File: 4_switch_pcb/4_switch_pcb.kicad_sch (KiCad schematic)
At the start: 11 parts, among them J1 USB_B_Micro, SW1 SW_Push, U1 ATmega32U4-A, Y1 Crystal_GND2_Small

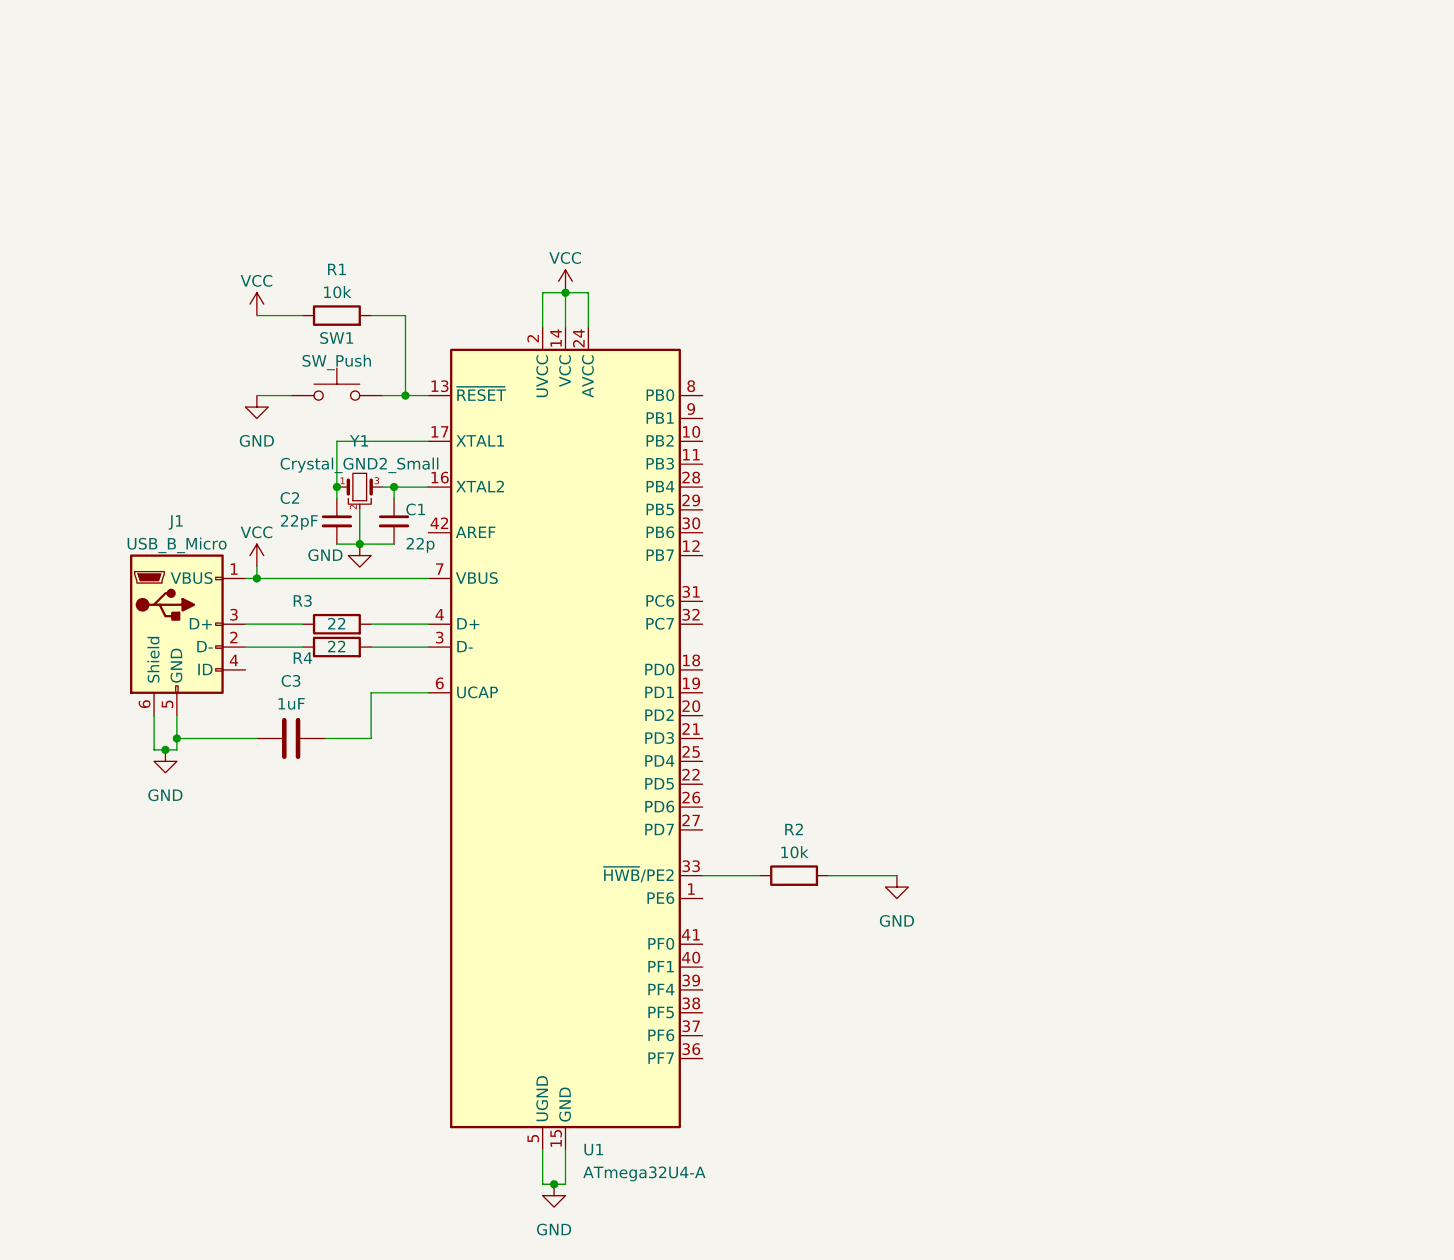
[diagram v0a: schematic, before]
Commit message: feat: add switch matrix, isp and header pins
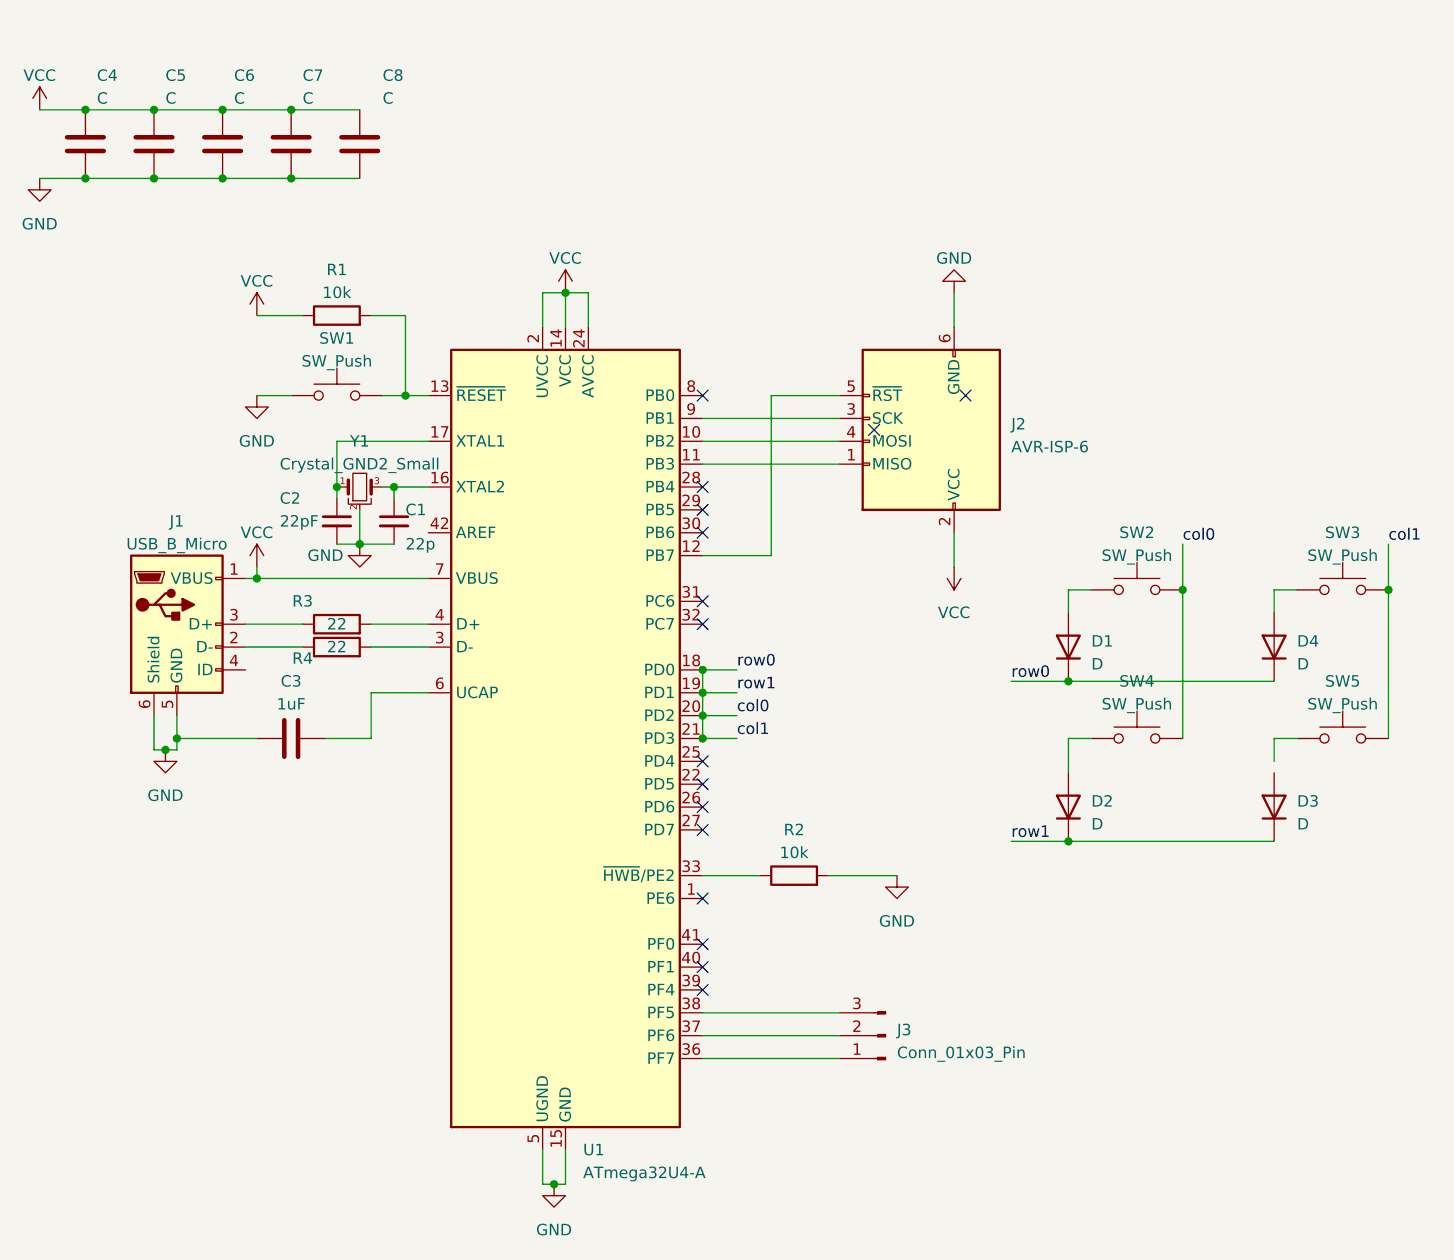
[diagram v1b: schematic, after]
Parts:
- added C4, C5, C6, C7, C8: C, symbol Device:C
- added D1, D2, D3, D4: D, symbol Device:D
- added J2: AVR-ISP-6, symbol Connector:AVR-ISP-6
- added J3: Conn_01x03_Pin, symbol Connector:Conn_01x03_Pin
- added SW2, SW3, SW4, SW5: SW_Push, symbol Switch:SW_Push
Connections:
- net GND: now also C4.2, C5.2, C6.2, C7.2, C8.2, J2.6 (GND)
- net VCC: now also C4.1, C5.1, C6.1, C7.1, C8.1, J2.2 (VCC)
- net at U1.10 (PB2): now also J2.4 (MOSI)
- net at U1.11 (PB3): now also J2.1 (MISO)
- net at U1.12 (PB7): now also J2.5 (~{RST})
- net col0: now reaches U1.18 (PD0)
- net col0: now also U1.19 (PD1), U1.20 (PD2), U1.21 (PD3), D1.1 (K), D2.1 (K), D3.1 (K), D4.1 (K), SW2.2, SW3.2, SW4.2, SW5.2
- net at U1.36 (PF7): now also J3.1 (Pin_1)
- net at U1.37 (PF6): now also J3.2 (Pin_2)
- net at U1.38 (PF5): now also J3.3 (Pin_3)
- net at U1.9 (PB1): now also J2.3 (SCK)
- new net: D2.2 (A), SW4.1
- new net: D1.2 (A), SW2.1
- new net: D4.2 (A), SW3.1
- no-connect marks 0 -> 16

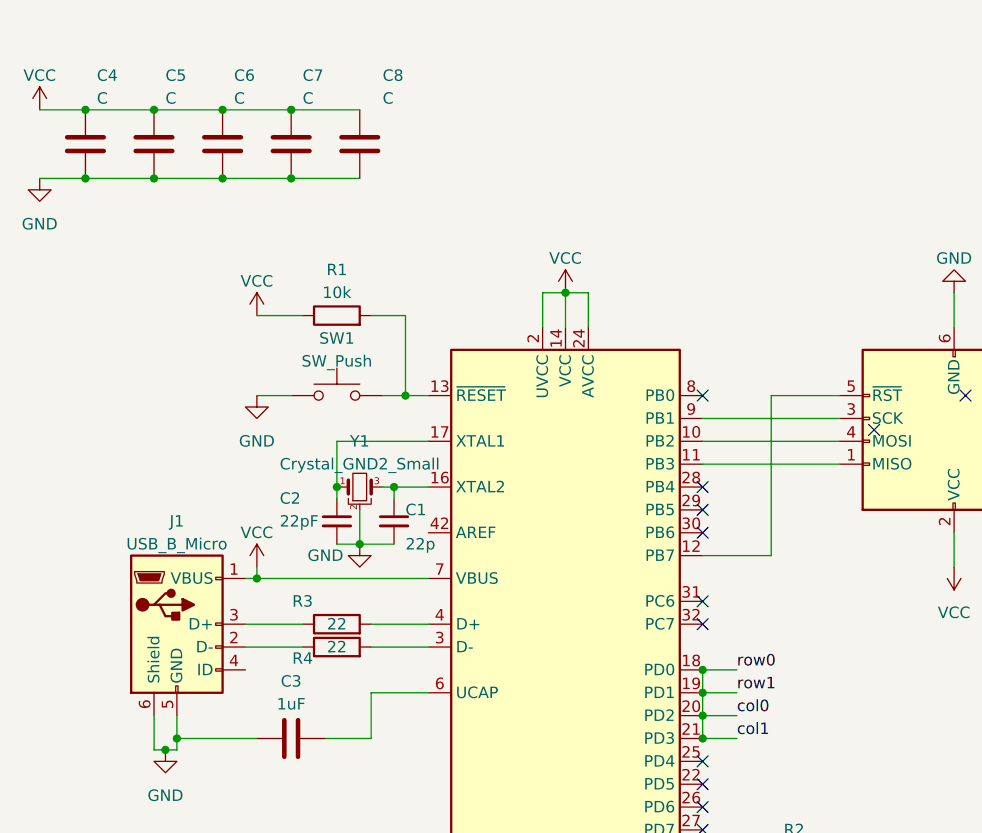
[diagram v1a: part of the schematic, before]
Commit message: feat: add decoupling value, missing vusb capa, crystal frequency
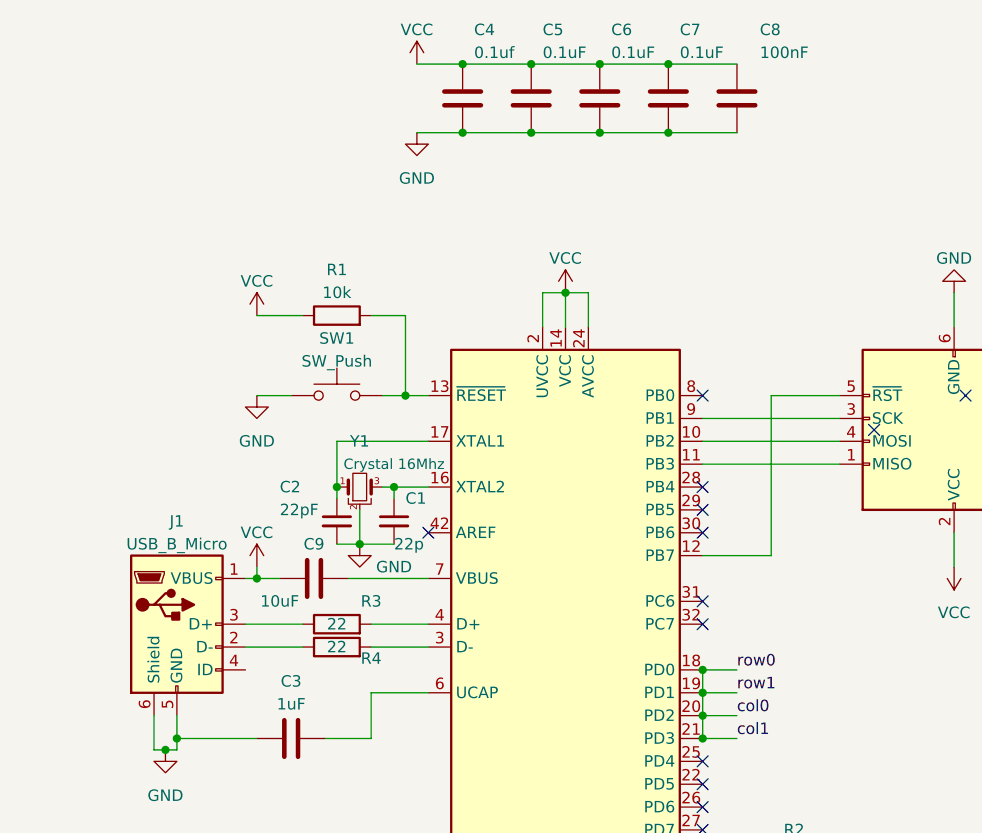
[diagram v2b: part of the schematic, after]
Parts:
- added C9: 10uF, symbol Device:C
- C4: value C -> 0.1uf
- C5, C6, C7: value C -> 0.1uF
- C8: value C -> 100nF
- Y1: value Crystal_GND2_Small -> Crystal 16Mhz
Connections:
- net VCC: now also C9.1; no longer U1.7 (VBUS)
- new net: C9.2, U1.7 (VBUS)
- no-connect marks 16 -> 17
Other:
- moved on the sheet: C4, C5, C6, C7, C8

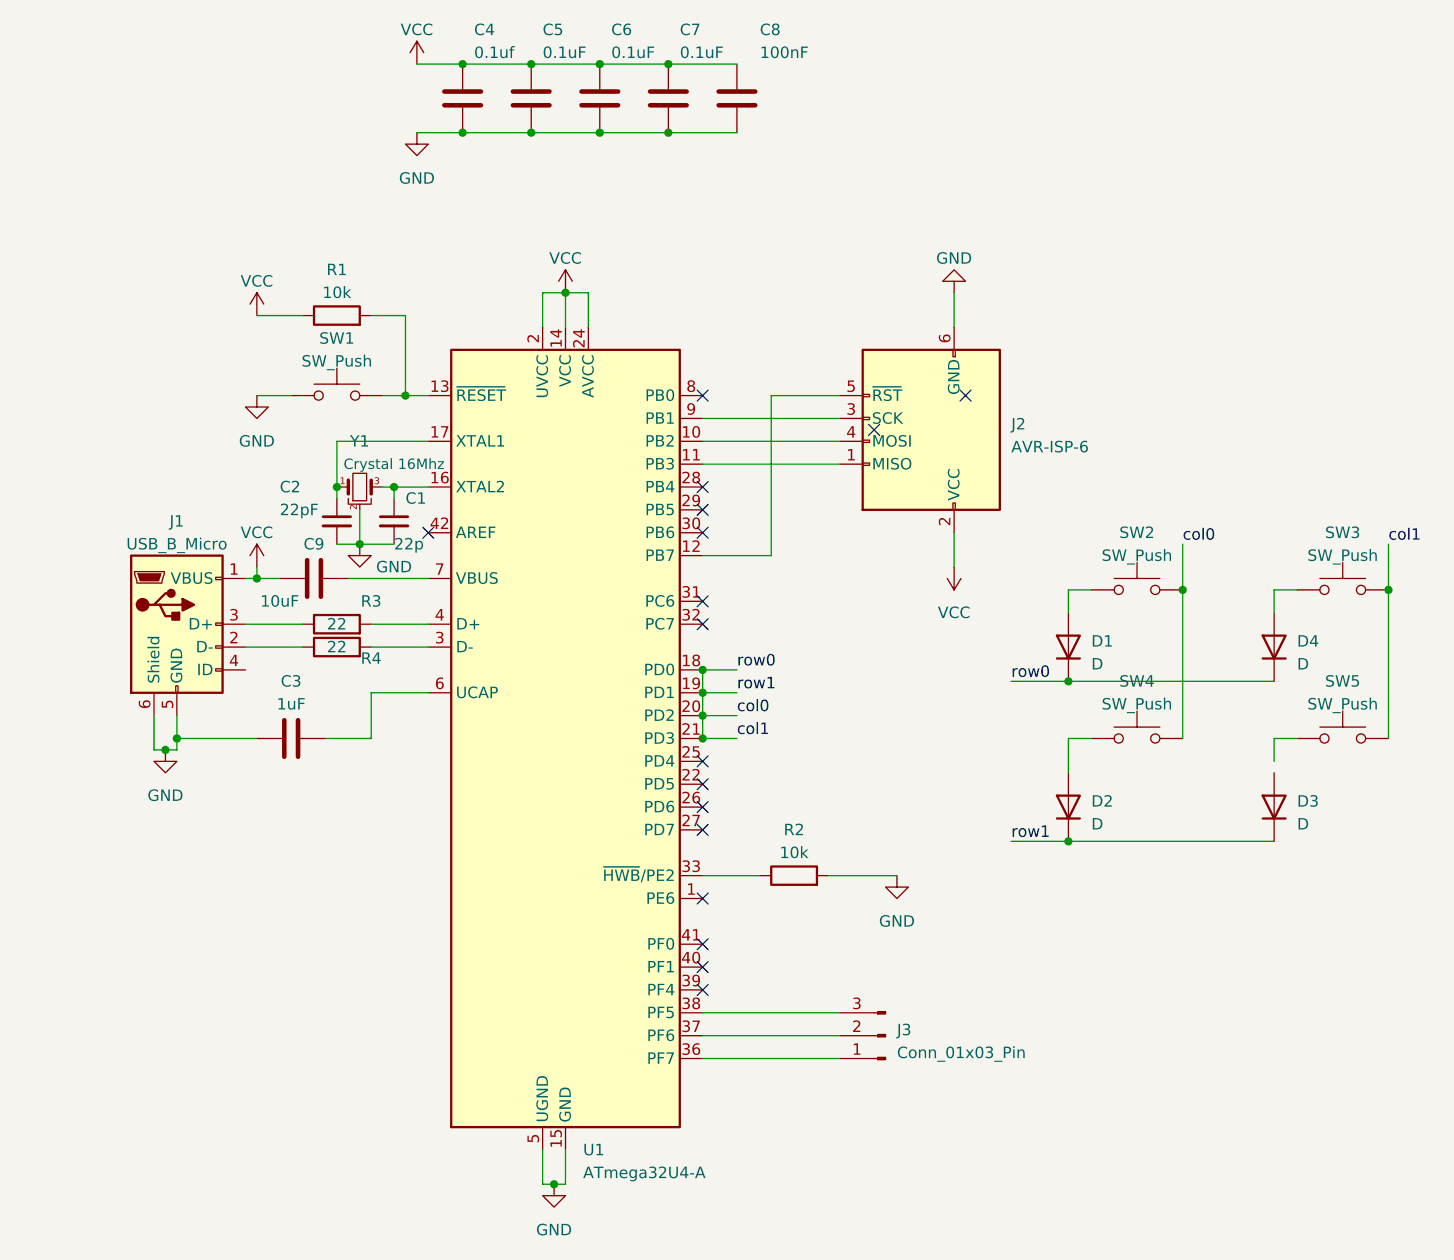
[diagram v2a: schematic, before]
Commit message: feat: add footprints selection
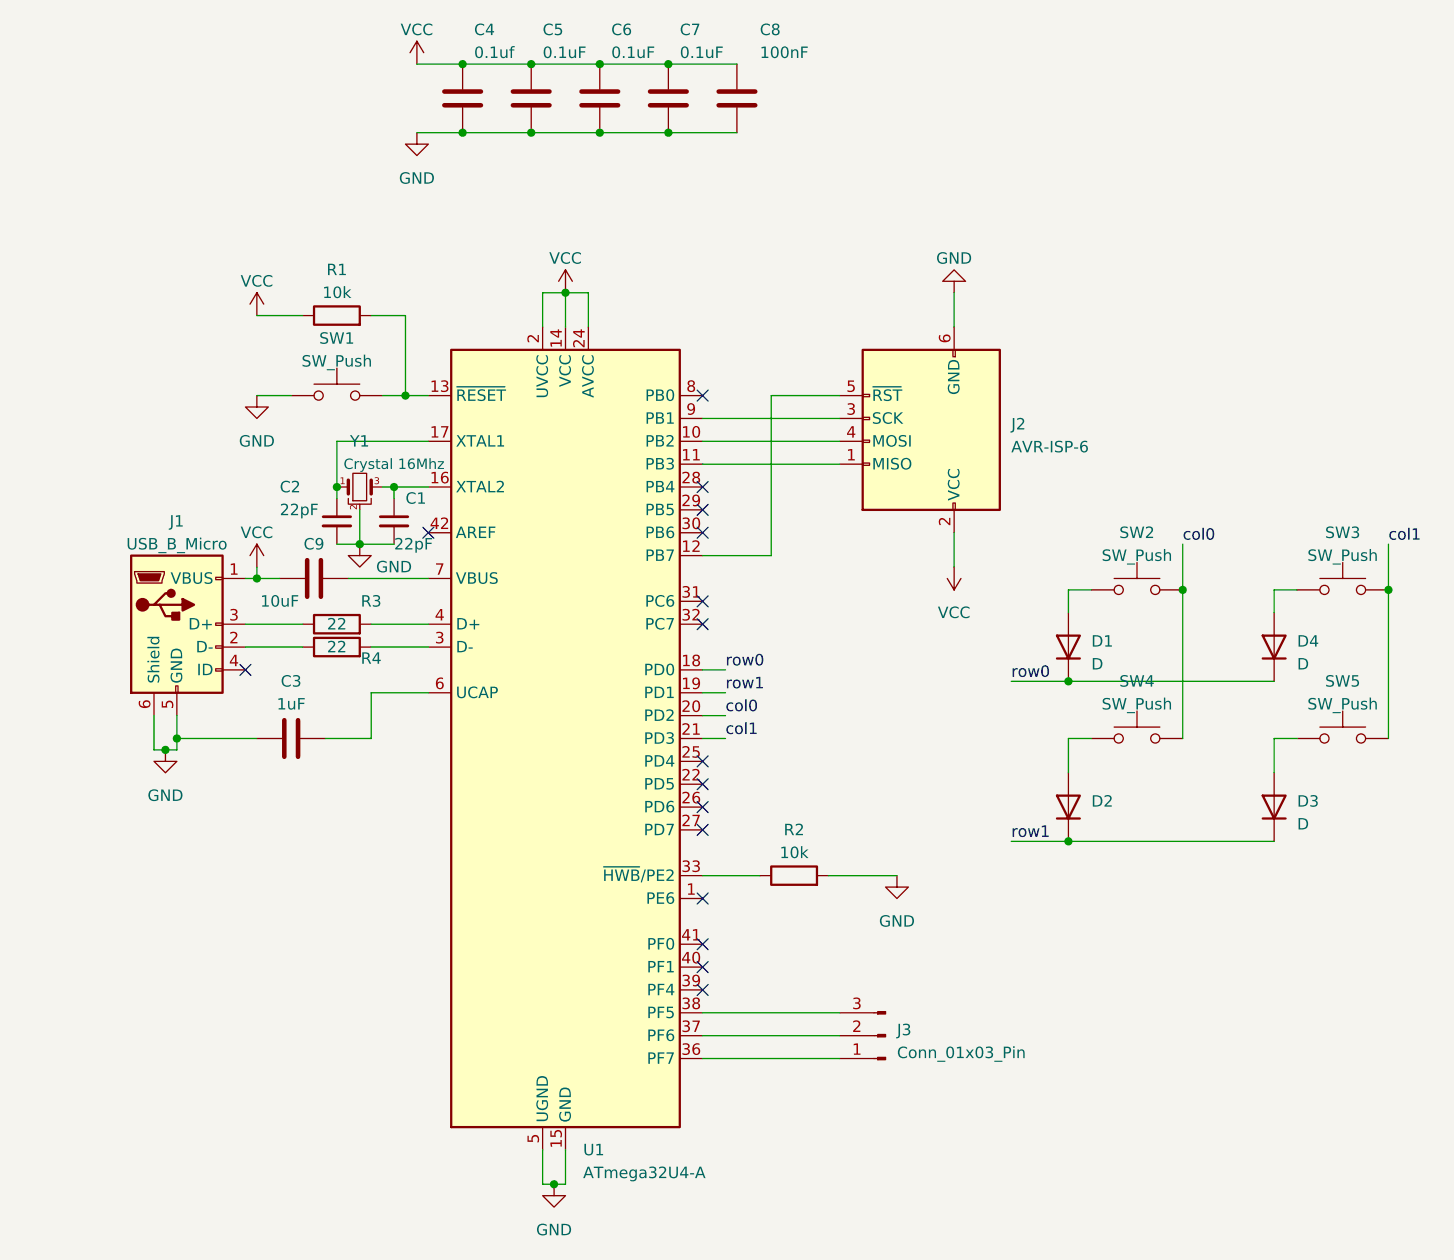
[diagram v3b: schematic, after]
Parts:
- C1: value 22p -> 22pF; footprint (none) -> Capacitor_SMD:C_0805_2012Metric_Pad1.18x1.45mm_HandSolder
- C2, C3, C4, C5, C6, C7, C8, C9: footprint (none) -> Capacitor_SMD:C_0805_2012Metric_Pad1.18x1.45mm_HandSolder
- D1, D2, D3, D4: footprint (none) -> keyboard_parts:D_SOD123_axial
- J1: footprint (none) -> keyboard_parts:USB_miniB_hirose_5S8
- J2: footprint (none) -> footprints:AVR-ISP-6
- J3: footprint (none) -> Connector_PinHeader_1.00mm:PinHeader_1x03_P1.00mm_Vertical_SMD_Pin1Right
- R1, R2, R3, R4: footprint (none) -> Resistor_SMD:R_0805_2012Metric_Pad1.20x1.40mm_HandSolder
- SW1: footprint (none) -> Button_Switch_SMD:SW_SPST_TL3342
- SW2, SW3, SW4, SW5: footprint (none) -> Button_Switch_Keyboard:SW_Cherry_MX_1.00u_PCB
- Y1: footprint (none) -> user:crystal_FA238-TSX3225
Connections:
- net col0: no longer D1.1 (K), D2.1 (K), D3.1 (K), D4.1 (K), SW3.2, SW5.2, U1.18 (PD0), U1.19 (PD1), U1.21 (PD3)
- net at D3.2 (A): now also SW5.1
- new net col1: SW3.2, SW5.2, U1.21 (PD3)
- new net row0: D1.1 (K), D4.1 (K), U1.18 (PD0)
- new net row1: D2.1 (K), D3.1 (K), U1.19 (PD1)
- no-connect marks 17 -> 16

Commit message: add base of routing
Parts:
- removed Y1: Crystal 16Mhz, user:crystal_FA238-TSX3225, symbol Device:Crystal_GND2_Small
- added X1: 16 MHZ, user:crystal_FA238-TSX3225, symbol keyboard_parts:XTAL_GND
- C8: value 100nF -> 4.7uF
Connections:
- net GND: now also X1.3
- net at C1.1, U1.16 (XTAL2): now also X1.2
- net at C2.1, U1.17 (XTAL1): now also X1.1
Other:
- moved on the sheet: C2
